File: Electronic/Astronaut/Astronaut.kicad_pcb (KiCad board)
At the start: 4 copper layers, 55 x 55 mm, 116 parts, among them J1 Conn_01x05, J2 Conn_01x04, J3 Conn_01x02, J4 Conn_01x02, J5 Conn_01x04, J6 Conn_01x04, J7 Conn_01x02, J8 Conn_01x10, J9 TC2050, SW1 SH-1808SN-250GF, SW2 SH-1808SN-250GF, U1 LAN8651B1-E/LMX, U10 ESP32-P4-MODULE-32MB, U11 ES8388, U12 TPS61169DCKR, U2 AVRH10C221KT1R5YA8, U3 AVRH10C221KT1R5YA8, U4 MCP2518FDT-E/SL, U5 ATA6563-GAQW1, U6 ESD5451N_C5261080, U7 ESD5451N_C5261080, U8 ADS1115IDGSR, U9 Core1106, X1 ABM10-25.000MHZ-D30-T3

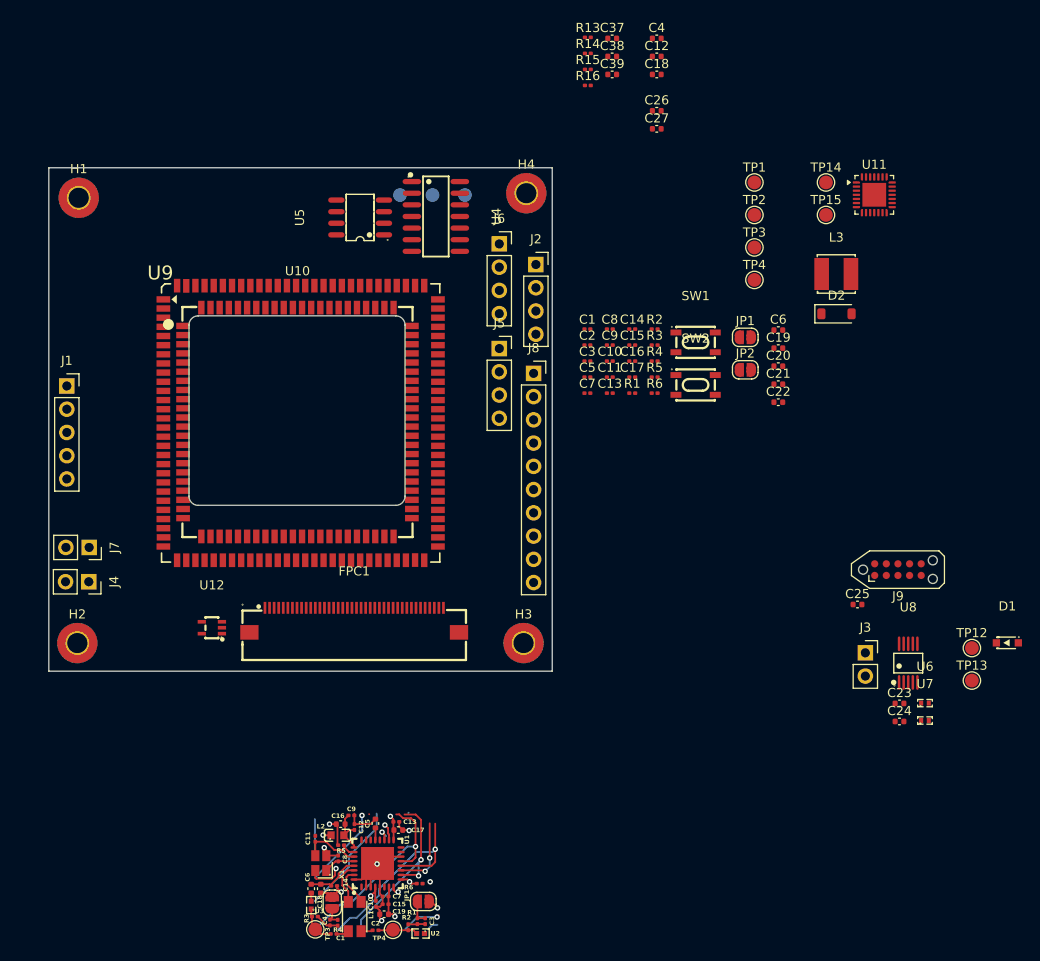
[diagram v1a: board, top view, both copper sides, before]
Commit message: WIP Astronaut : completed most of the routing / schematic : next audio / power protection
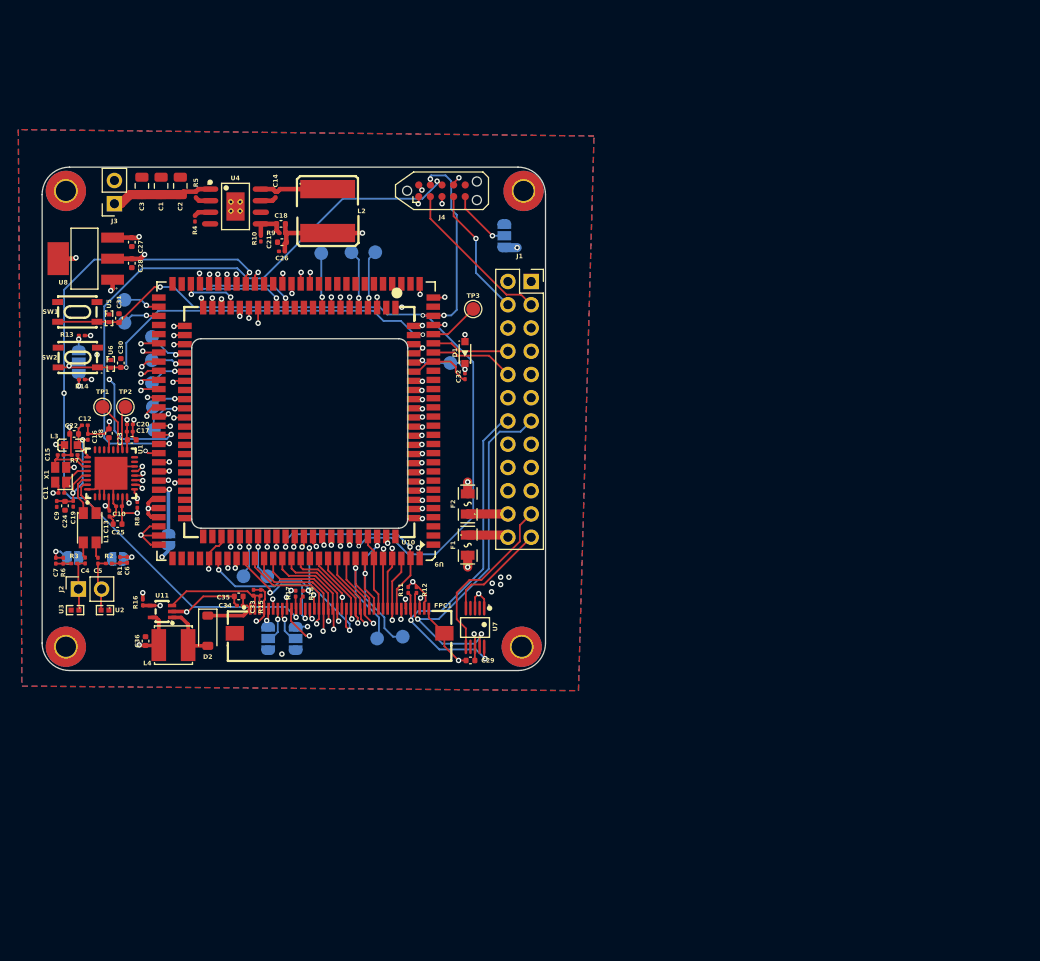
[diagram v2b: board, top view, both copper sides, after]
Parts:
- removed the C10 at (108.5, 51.7)
- removed the C11 at (108.5, 53.4)
- removed the C12 at (113.7, 18.4)
- removed the C13 at (108.5, 55.2)
- removed the C15 at (84.0, 111.0)
- removed the C15 at (111.0, 49.9)
- removed the C16 at (111.0, 51.7)
- removed the C19 at (126.9, 50.3)
- removed the C20 at (126.9, 52.2)
- removed the C22 at (126.9, 56.2)
- removed the C25 at (135.6, 78.3)
- removed the C4 at (113.7, 16.4)
- removed the C5 at (106.1, 53.4)
- removed the C6 at (126.9, 48.3)
- removed the C7 at (106.1, 55.2)
- removed the C8 at (108.5, 48.2)
- removed the C9 at (108.5, 49.9)
- removed the J2 at (100.5, 41.1)
- removed the J4 at (51.6, 75.8)
- removed J5, J6: Conn_01x04, Connector_PinSocket_2.54mm:PinSocket_1x04_P2.54mm_Vertical
- removed J8: Conn_01x10, Connector_PinSocket_2.54mm:PinSocket_1x10_P2.54mm_Vertical
- removed the JP1 at (123.3, 49.1)
- removed the JP2 at (123.3, 52.6)
- removed the R1 at (111.0, 55.2)
- removed the R2 at (113.4, 48.2)
- removed the R3 at (113.4, 49.9)
- removed the R6 at (113.4, 55.2)
- removed the TP3 at (76.3, 113.8)
- removed the TP3 at (124.3, 39.3)
- removed the TP4 at (124.3, 42.8)
- removed the TP4 at (84.8, 113.8)
- removed the U11 at (137.4, 33.5)
- removed the U5 at (81.2, 36.0)
- added C28: 10uF, Capacitor_SMD:C_0402_1005Metric, F.Cu at (56.3, 41.0)
- added C31: 0.1uF, Capacitor_SMD:C_0402_1005Metric, F.Cu at (54.9, 47.0)
- added C32: 1uF, Capacitor_SMD:C_0201_0603Metric, F.Cu at (92.7, 53.3)
- added C36: 10uF, Capacitor_SMD:C_0402_1005Metric, F.Cu at (57.8, 82.3)
- added F1: BSMD0805-110-6V, lcsc:F0805, F.Cu at (93.0, 71.8)
- added F2: BSMD0805-110-6V, lcsc:F0805, F.Cu at (93.0, 67.3)
- added JP3: Jumper_3_Open, Jumper:SolderJumper-3_P1.3mm_Open_RoundedPad1.0x1.5mm_NumberLabels, B.Cu at (50.5, 51.8)
- added JP4: Jumper_3_Open, Jumper:SolderJumper-3_P1.3mm_Open_RoundedPad1.0x1.5mm_NumberLabels, B.Cu at (97.0, 38.0)
- added JP5: Jumper_2_Open, Jumper:SolderJumper-2_P1.3mm_Open_RoundedPad1.0x1.5mm, B.Cu at (60.3, 71.2)
- added JP6: Jumper, Jumper:SolderJumper-3_P1.3mm_Open_RoundedPad1.0x1.5mm_NumberLabels, B.Cu at (74.2, 82.0)
- added JP7: Jumper, Jumper:SolderJumper-3_P1.3mm_Open_RoundedPad1.0x1.5mm_NumberLabels, B.Cu at (71.2, 82.0)
- added L2: NR6045T100M, lcsc:IND-SMD_L6.0-W6.0_NR6045, F.Cu at (77.7, 35.3)
- added R10: 20K, Resistor_SMD:R_0201_0603Metric, F.Cu at (70.4, 38.3)
- added R11: 10K, Resistor_SMD:R_0201_0603Metric, F.Cu at (86.5, 76.7)
- added R12: 10K, Resistor_SMD:R_0201_0603Metric, F.Cu at (87.4, 76.7)
- added R13: 10K, Resistor_SMD:R_0201_0603Metric, F.Cu at (50.8, 48.9)
- added R14: 10K, Resistor_SMD:R_0201_0603Metric, F.Cu at (50.8, 53.7)
- added R9: 105K, Resistor_SMD:R_0201_0603Metric, F.Cu at (72.7, 37.7)
- added TP10: TestPoint, TestPoint:TestPoint_Pad_D1.5mm, B.Cu at (58.7, 59.2)
- added TP18: TestPoint, TestPoint:TestPoint_Pad_D1.5mm, B.Cu at (91.1, 51.9)
- added TP3: TestPoint, TestPoint:TestPoint_Pad_D1.5mm, F.Cu at (93.6, 46.0)
- added TP4: TestPoint, TestPoint:TestPoint_Pad_D1.5mm, B.Cu at (55.5, 47.5)
- added TP5: TestPoint, TestPoint:TestPoint_Pad_D1.5mm, B.Cu at (55.5, 45.0)
- added TP6: TestPoint, TestPoint:TestPoint_Pad_D1.5mm, B.Cu at (58.5, 49.0)
- added TP7: TestPoint, TestPoint:TestPoint_Pad_D1.5mm, B.Cu at (58.5, 51.6)
- added TP8: TestPoint, TestPoint:TestPoint_Pad_D1.5mm, B.Cu at (58.5, 54.1)
- added TP9: TestPoint, TestPoint:TestPoint_Pad_D1.5mm, B.Cu at (58.6, 56.7)
- added U8: NCP1117ST33T3G, lcsc:SOT-223-3_L6.5-W3.4-P2.30-LS7.0-BR, F.Cu at (51.2, 40.5)
- C1, C2: value 0.1uF -> 1uF/100V; footprint Capacitor_SMD:C_0201_0603Metric -> Capacitor_SMD:C_0805_2012Metric
- C14: value 10nF -> 0.1uF/25V
- C18: value 0.1uF -> 22uF/25V
- C21: value 10uF -> 22uF/25V
- C26: value 0.1uF -> 220pF; footprint Capacitor_SMD:C_0402_1005Metric -> Capacitor_SMD:C_0201_0603Metric
- C27: value 0.1uF -> 10uF
- C3: value 0.1uF -> 0.1uF/100V; footprint Capacitor_SMD:C_0201_0603Metric -> Capacitor_SMD:C_0805_2012Metric
- C33: renamed from C37; footprint Capacitor_SMD:C_0402_1005Metric -> Capacitor_SMD:C_0201_0603Metric
- C34: renamed from C38; footprint Capacitor_SMD:C_0402_1005Metric -> Capacitor_SMD:C_0201_0603Metric
- C9: renamed from C6; footprint Capacitor_SMD:C_0402_1005Metric -> Capacitor_SMD:C_0201_0603Metric
- J1: value Conn_01x05 -> Conn_02x12_Counter_Clockwise; footprint Connector_PinSocket_2.54mm:PinSocket_1x05_P2.54mm_Vertical -> Connector_PinSocket_2.54mm:PinSocket_2x12_P2.54mm_Vertical
- JP1, JP2: moved to B.Cu
- R4: value 100K -> 200K
- R5: value 12.4K 1% -> 1M
- TP14: renamed from TP12; moved to B.Cu
- TP15: renamed from TP13; moved to B.Cu
- TP16: renamed from TP14; moved to B.Cu
- TP17: renamed from TP15; moved to B.Cu
- U4: value MCP2518FDT-E/SL -> SY8513FCC; footprint lcsc:SOIC-14_L8.7-W3.9-P1.27-LS6.0-BL -> lcsc:SOP-8_L4.9-W3.9-P1.27-LS6.0-BL-EP3.1
- moved U5 98.6 mm to (53.8, 47.0), turned to -90 degrees
- moved U6 97.1 mm to (54.0, 52.0), turned to -90 degrees
- moved C30 93.7 mm to (55.1, 51.9), turned to 90 degrees
- moved J2 86.3 mm to (50.5, 76.6), turned to 90 degrees
- moved L4 83.0 mm to (60.9, 82.7), turned to 180 degrees
- moved TP15 80.4 mm to (68.5, 75.2), turned to 180 degrees
- moved TP14 77.4 mm to (71.1, 75.2), turned to 180 degrees
- moved R16 77.2 mm to (57.5, 78.1), turned to -90 degrees
- moved D2 76.9 mm to (64.6, 81.2), turned to -90 degrees
- moved TP1 75.3 mm to (53.1, 56.7)
- moved C34 72.5 mm to (68.1, 78.4), turned to 180 degrees
- moved C33 72.1 mm to (69.6, 77.0), turned to 90 degrees
- moved TP2 71.9 mm to (55.6, 56.7)
- moved R15 70.4 mm to (70.4, 77.0), turned to 90 degrees
- moved C35 70.1 mm to (68.0, 77.4), turned to 180 degrees
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- renumbered C7 to C10, C8 to C11, C9 to C12, C10 to C13, C11 to C15, C12 to C16, C13 to C17, C14 to C19, C17 to C20, C16 to C22, C17 to C23, C18 to C24, C19 to C25, C23 to C29, C24 to C30, C39 to C35, C1 to C4, C2 to C5, C3 to C6, C4 to C7, C5 to C8, J3 to J2, J7 to J3, J9 to J4, L2 to L3, L3 to L4, R13 to R15, R14 to R16, R15 to R17, R16 to R18, R4 to R6, R5 to R7, R6 to R8, TP9 to TP11, TP10 to TP12, TP11 to TP13, U12 to U11, U6 to U5, U7 to U6, U8 to U7
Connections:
- C1 pad 1: Net-(C1-Pad1) -> +12V
- C1 pad 2: Net-(C1-Pad2) -> GND
- C10 pad 1: +3V3 -> +3.3V
- C13 pad 1: +3V3 -> +3.3V
- C14 pad 1: Net-(U1-VDDA) -> Net-(U4-BS)
- C14 pad 2: GND -> Net-(U4-LX)
- C17 pad 1: +3V3 -> +3.3V
- C18 pad 1: +3.3V -> +5V
- C18 pad 2: GND -> Net-(U4-FB)
- C2 pad 1: Net-(C2-Pad1) -> +12V
- C2 pad 2: Net-(C2-Pad2) -> GND
- C20 pad 1: +3V3 -> +3.3V
- C21 pad 1: Net-(U1-VDDA) -> +5V
- C23 pad 1: +3V3 -> +3.3V
- C25 pad 1: +3V3 -> +3.3V
- C26 pad 1: /CAN_INT -> +5V
- C27 pad 1: /ESP32-P4 + C6/ADC1_CHANEL5 -> +5V
- C3 pad 1: Net-(C3-Pad1) -> +12V
- C3 pad 2: Net-(JP1-B) -> GND
- C4 pad 1: Net-(C1-Pad1) -> Net-(J2-Pin_1)
- C4 pad 2: Net-(C1-Pad2) -> Net-(C4-Pad2)
- C5 pad 1: Net-(C2-Pad1) -> Net-(J2-Pin_2)
- C5 pad 2: Net-(C2-Pad2) -> Net-(C5-Pad2)
- C6 pad 1: Net-(C3-Pad1) -> Net-(C6-Pad1)
- J1 pad 1: +3.3V -> /GPIO_03
- J1 pad 2: /SPI_MISO -> /GPIO_04
- J1 pad 3: /SPI_MOSI -> /GPIO_06
- J1 pad 4: /SPI_CLK -> /GPIO_05
- J1 pad 5: GND -> /GPIO_02
- J2 pad 1: /TRX_P -> Net-(J2-Pin_1)
- J2 pad 2: /TRX_N -> Net-(J2-Pin_2)
- J4 pad 1: unconnected-(J9-Pad1) -> +3.3V
- J4 pad 10: unconnected-(J9-Pad10) -> /BUTTON2
- J4 pad 2: unconnected-(J9-Pad2) -> /GPIO_06
- J4 pad 3: unconnected-(J9-Pad3) -> GND
- J4 pad 4: unconnected-(J9-Pad4) -> /GPIO_05
- J4 pad 5: unconnected-(J9-Pad5) -> Net-(JP4-C)
- J4 pad 7: unconnected-(J9-Pad7) -> /Core1106/JTAG_MCU_TCK
- J4 pad 8: unconnected-(J9-Pad8) -> /Core1106/JTAG_MCU_TMS
- J4 pad 9: unconnected-(J9-Pad9) -> /BUTTON1
- L1 pad 2: Net-(C1-Pad2) -> Net-(C4-Pad2)
- L1 pad 3: Net-(C2-Pad2) -> Net-(C5-Pad2)
- L3 pad 1: +3V3 -> +3.3V
- R1 pad 1: Net-(C3-Pad1) -> Net-(C6-Pad1)
- R2 pad 1: Net-(C2-Pad1) -> Net-(J2-Pin_2)
- R2 pad 2: Net-(C3-Pad1) -> Net-(C6-Pad1)
- R3 pad 1: Net-(C1-Pad1) -> Net-(J2-Pin_1)
- R4 pad 1: Net-(C5-Pad1) -> Net-(U4-FS)
- R4 pad 2: Net-(JP2-B) -> GND
- R5 pad 1: Net-(U1-RBIAS) -> Net-(U4-EN)
- R5 pad 2: GND -> +12V
- R8 pad 2: +3V3 -> +3.3V
- U1 pad 17: +3V3 -> +3.3V
- U1 pad 4: +3V3 -> +3.3V
- U1 pad 7: +3V3 -> +3.3V
- U10 pad 13: /GPIO_03 -> /GPIO_06
- U10 pad 14: /GPIO_02 -> /GPIO_04
- U10 pad 19: /GPIO_01 -> /GPIO_03
- U10 pad 29: /CAN_INT -> /TFT_CS
- U10 pad 30: /ESP32-P4 + C6/ADC1_CHANEL5 -> /ESP32-P4 + C6/GPIO21
- U10 pad 6: /ESP32-P4 + C6/C6_IO15 -> /GPIO_01
- U10 pad 7: /GPIO_06 -> /GPIO_02
- U10 pad 88: /CAN_CS -> /GPIO_07
- U2 pad 2: Net-(C2-Pad1) -> Net-(J2-Pin_2)
- U3 pad 1: Net-(C1-Pad1) -> Net-(J2-Pin_1)
- U4 pad 1: Net-(U4-TXCAN) -> +12V
- U4 pad 2: Net-(U4-RXCAN) -> Net-(U4-EN)
- U4 pad 3: unconnected-(U4-CLKO/SOF-Pad3) -> Net-(U4-FS)
- U4 pad 4: /CAN_INT -> GND
- U4 pad 5: unconnected-(U4-OSC2-Pad5) -> Net-(U4-FB)
- U4 pad 6: unconnected-(U4-OSC1-Pad6) -> /PG
- U4 pad 7: GND -> Net-(U4-BS)
- U4 pad 8: /CAN_INT1 -> Net-(U4-LX)
- U4 pad 9: /CAN_INT0 -> GND
- U7 pad 6: /ADC4 -> /ADC2
- U9 pad 24: unconnected-(U9-USB_VBUSDET-Pad24) -> Net-(U9-USB_VBUSDET)
- U9 pad 41: /CAN_CS -> /GPIO_07
- U9 pad 72: Net-(U9-JTAG_CPU_TCK_M1/UART2_TX_M1/JTAG_HPMCU_TCK_M0/JTAG_LPMCU_TCK_M0/GPIO1_B2_d) -> /Core1106/JTAG_MCU_TCK
- U9 pad 73: Net-(U9-JTAG_CPU_TMS_M1/UART2_RX_M1/JTAG_HPMCU_TMS_M0/JTAG_LPMCU_TMS_M0/GPIO1_B3_u) -> /Core1106/JTAG_MCU_TMS
- U9 pad 78: +3.3V -> Net-(JP5-A)
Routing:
- net +5V: track 0.00 -> 171.6 mm, vias 0 -> 6
- net /I2C_SDA: track 0.00 -> 109.6 mm, vias 0 -> 4
- net /BUTTON1: track 0.00 -> 105.6 mm, vias 0 -> 5
- net /I2C_SCL: track 0.00 -> 102.7 mm, vias 0 -> 4
- net /SPI_CLK: track 22.7 -> 117.5 mm, vias 1 -> 4
- net /TFT_CS: track 0.00 -> 93.7 mm, vias 0 -> 4
- net /TP_IRQ: track 0.00 -> 92.0 mm, vias 0 -> 4
- net /BUTTON2: track 0.00 -> 80.9 mm, vias 0 -> 5
- net /UART1_RX: track 0.00 -> 74.7 mm, vias 0 -> 2
- net /UART1_TX: track 0.00 -> 73.4 mm, vias 0 -> 2
- net /SPI_MOSI: track 22.7 -> 95.9 mm, vias 1 -> 4
- net /RST: track 0.00 -> 72.9 mm, vias 0 -> 4
- net /GPIO_06: track 0.00 -> 69.4 mm, vias 0 -> 2
- net /SPI_MISO: track 20.6 -> 89.4 mm, vias 2 -> 3
- net /UART2_TX: track 0.00 -> 68.4 mm, vias 0 -> 2
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- added copper zone on In2.Cu, net +3.3V
- added copper zone on B.Cu, net GND
- added copper zone on F.Cu, net GND
- added copper zone on In1.Cu, net GND
- added copper zone on In4.Cu, net GND
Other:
- outline, holes or cut-outs redrawn
- copper layers 4 -> 6
